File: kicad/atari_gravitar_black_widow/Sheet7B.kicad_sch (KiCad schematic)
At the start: 37 parts, among them Q10 2N3904, Q5 2N3904, Q6 2N3904, Q7 2N3906, Q8 2N3904, Q9 2N3904

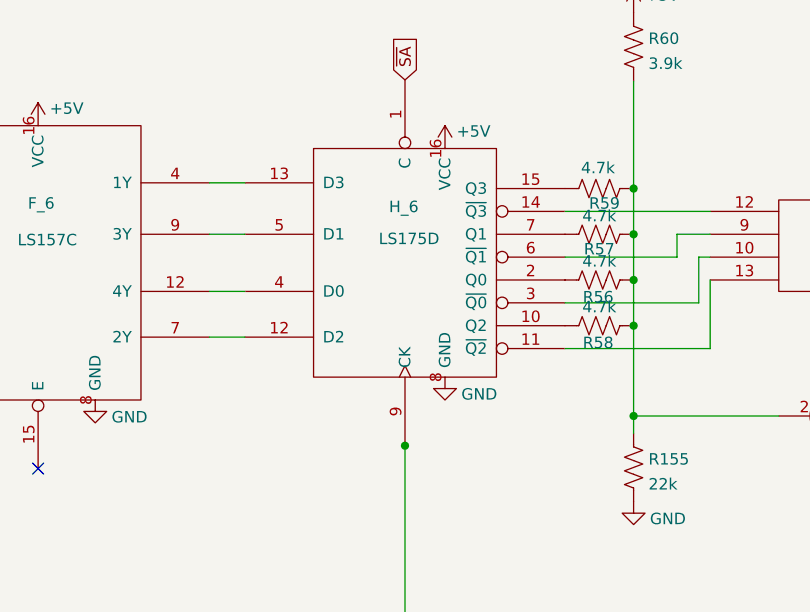
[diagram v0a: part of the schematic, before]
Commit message: Removed more warnings - 25 warnings remain
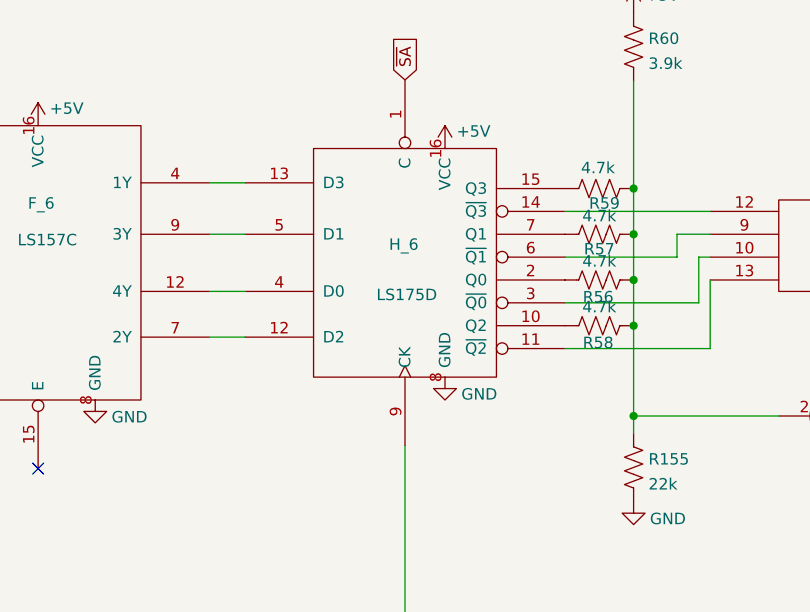
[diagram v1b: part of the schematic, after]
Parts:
- Q10, Q5, Q6, Q7, Q8, Q9: footprint TO_SOT_Packages_THT:TO-92_Molded_Narrow -> (none)

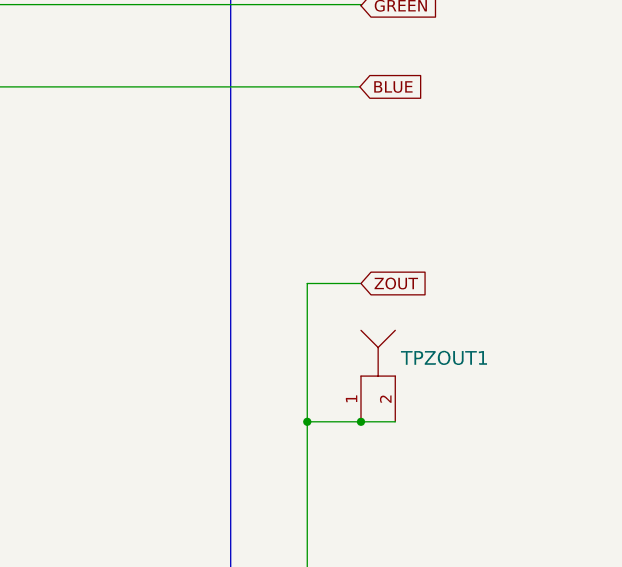
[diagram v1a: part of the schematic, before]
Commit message: 20 warnings left kicad 6.0
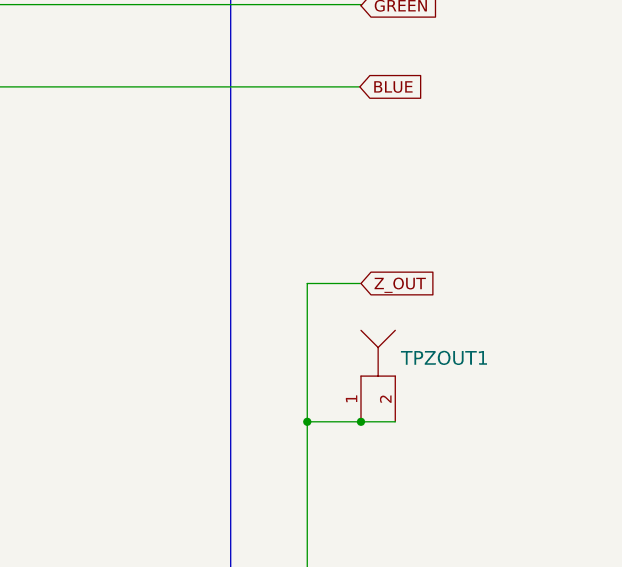
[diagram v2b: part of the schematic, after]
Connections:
- net ZOUT renamed Z_OUT
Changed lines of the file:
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@@
     )
   )
-  (global_label "ZOUT" (shape input) (at 521.208 181.356 0) (fields_autoplaced)
+  (global_label "Z_OUT" (shape input) (at 521.208 181.356 0) (fields_autoplaced)
     (effects (font (size 1.27 1.27)) (justify left))
-    (property "Intersheet References" "${INTERSHEET_REFS}" (id 0) (at 528.3703 181.2766 0)
+    (property "Intersheet References" "${INTERSHEET_REFS}" (id 0) (at 529.3379 181.2766 0)
       (effects (font (size 1.27 1.27)) (justify left) hide)
     )

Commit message: all warnings mitigated!!
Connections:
- net ~{Z0} is gone; now on net Z0: F_5.13
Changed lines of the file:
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@@
     )
   )
-  (global_label "~{Z0}" (shape input) (at 40.64 269.113 180) (fields_autoplaced)
+  (global_label "Z0" (shape input) (at 40.64 269.113 180) (fields_autoplaced)
     (effects (font (size 1.27 1.27)) (justify right))
     (property "Intersheet References" "${INTERSHEET_REFS}" (id 0) (at 35.8968 269.0336 0)

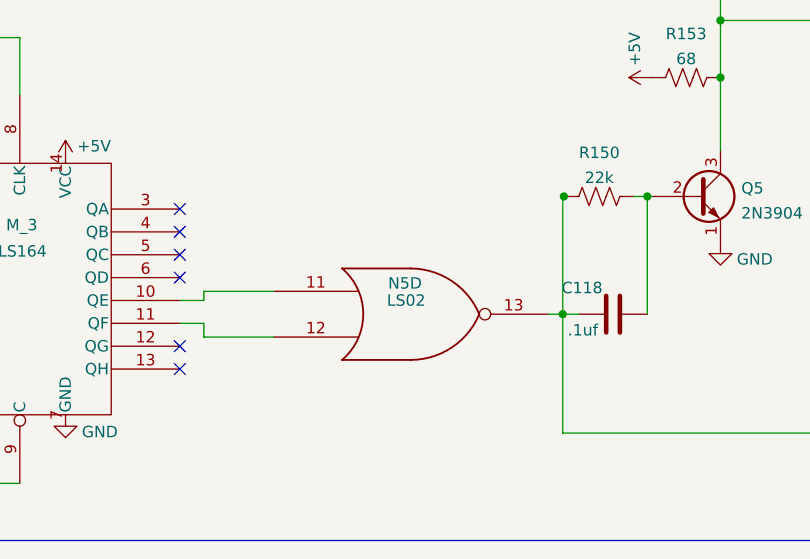
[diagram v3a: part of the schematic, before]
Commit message: Fixed all warnings and errors
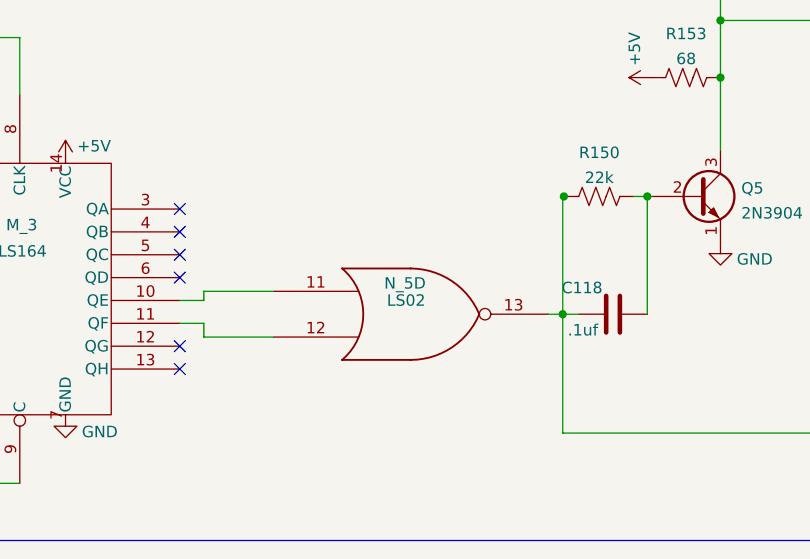
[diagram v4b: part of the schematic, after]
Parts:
- renumbered N5 to N_5
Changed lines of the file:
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@@
   (symbol (lib_id "Asteroids:LS02") (at 188.722 308.229 0) (unit 4)
     (in_bom yes) (on_board yes)
-    (property "Reference" "N5" (id 0) (at 188.087 304.8 0))
+    (property "Reference" "N_5" (id 0) (at 188.087 304.8 0))
     (property "Value" "LS02" (id 1) (at 188.214 306.705 0))
     (property "Footprint" "" (id 2) (at 188.722 308.229 0)

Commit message: more ttl placements
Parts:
- E_6, F_6, H_6: footprint (none) -> Star_Wars_Vector_PCB:DIP16
- F_5, H_5: footprint (none) -> Star_Wars_Vector_PCB:DIP14
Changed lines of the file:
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@@
       (effects (font (size 1.27 1.27)) (justify left))
     )
-    (property "Footprint" "" (id 2) (at 73.914 231.013 0)
+    (property "Footprint" "Star_Wars_Vector_PCB:DIP16" (id 2) (at 73.914 231.013 0)
       (effects (font (size 1.27 1.27)) hide)
     )
@@
       (effects (font (size 1.27 1.27)) (justify left))
     )
-    (property "Footprint" "" (id 2) (at 121.793 232.283 0)
+    (property "Footprint" "Star_Wars_Vector_PCB:DIP16" (id 2) (at 121.793 232.283 0)
       (effects (font (size 1.27 1.27)) hide)
     )
@@
     (property "Reference" "F_5" (id 0) (at 91.821 263.906 0))
     (property "Value" "LS11" (id 1) (at 91.694 266.827 0))
-    (property "Footprint" "" (id 2) (at 92.202 265.303 0)
+    (property "Footprint" "Star_Wars_Vector_PCB:DIP14" (id 2) (at 92.202 265.303 0)
       (effects (font (size 1.27 1.27)) hide)
     )
@@
       (effects (font (size 1.27 1.27)) (justify left))
     )
-    (property "Footprint" "" (id 2) (at 162.56 231.648 0)
+    (property "Footprint" "Star_Wars_Vector_PCB:DIP16" (id 2) (at 162.56 231.648 0)
       (effects (font (size 1.27 1.27)) hide)
     )
@@
     (property "Reference" "H_5" (id 0) (at 211.455 227.584 0))
     (property "Value" "LS20" (id 1) (at 211.455 229.997 0))
-    (property "Footprint" "" (id 2) (at 211.709 230.378 0)
-      (effects (font (size 1.27 1.27)) hide)
-    )
+    (property "Footprint" "Star_Wars_Vector_PCB:DIP14" (id 2) (at 211.709 230.378 0)
+      (effects (font (size 1.27 1.27)) hide)
+    )

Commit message: more chip layouts
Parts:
- J_3: footprint (none) -> Star_Wars_Vector_PCB:DIP14
- K_10: footprint (none) -> Star_Wars_Vector_PCB:DIP16
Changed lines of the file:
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@@
       (effects (font (size 1.27 1.27)) (justify left))
     )
-    (property "Footprint" "" (id 2) (at 330.073 207.772 0)
+    (property "Footprint" "Star_Wars_Vector_PCB:DIP16" (id 2) (at 330.073 207.772 0)
       (effects (font (size 1.27 1.27)) hide)
     )
@@
     (property "Reference" "J_3" (id 0) (at 245.364 225.425 0))
     (property "Value" "LS04" (id 1) (at 245.364 227.711 0))
-    (property "Footprint" "" (id 2) (at 242.189 230.378 0)
-      (effects (font (size 1.27 1.27)) hide)
-    )
+    (property "Footprint" "Star_Wars_Vector_PCB:DIP14" (id 2) (at 242.189 230.378 0)
+      (effects (font (size 1.27 1.27)) hide)
+    )

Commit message: placements
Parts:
- L_10, M_3, M_5, N_5: footprint (none) -> Star_Wars_Vector_PCB:DIP14
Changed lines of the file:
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@@
     (property "Reference" "L_10" (id 0) (at 362.839 201.2655 0))
     (property "Value" "74LS33" (id 1) (at 362.839 204.0406 0))
-    (property "Footprint" "" (id 2) (at 362.839 209.042 0)
+    (property "Footprint" "Star_Wars_Vector_PCB:DIP14" (id 2) (at 362.839 209.042 0)
       (effects (font (size 1.27 1.27)) hide)
     )
@@
     (property "Reference" "L_10" (id 0) (at 362.839 214.8545 0))
     (property "Value" "74LS33" (id 1) (at 362.839 217.6296 0))
-    (property "Footprint" "" (id 2) (at 362.839 222.631 0)
+    (property "Footprint" "Star_Wars_Vector_PCB:DIP14" (id 2) (at 362.839 222.631 0)
       (effects (font (size 1.27 1.27)) hide)
     )
@@
     (property "Reference" "L_10" (id 0) (at 362.966 228.5705 0))
     (property "Value" "74LS33" (id 1) (at 362.966 231.3456 0))
-    (property "Footprint" "" (id 2) (at 362.966 236.347 0)
+    (property "Footprint" "Star_Wars_Vector_PCB:DIP14" (id 2) (at 362.966 236.347 0)
       (effects (font (size 1.27 1.27)) hide)
     )
@@
     (property "Reference" "N_5" (id 0) (at 188.087 304.8 0))
     (property "Value" "LS02" (id 1) (at 188.214 306.705 0))
-    (property "Footprint" "" (id 2) (at 188.722 308.229 0)
+    (property "Footprint" "Star_Wars_Vector_PCB:DIP14" (id 2) (at 188.722 308.229 0)
       (effects (font (size 1.27 1.27)) hide)
     )
@@
       (effects (font (size 1.27 1.27)) (justify left))
     )
-    (property "Footprint" "" (id 2) (at 145.288 305.435 0)
+    (property "Footprint" "Star_Wars_Vector_PCB:DIP14" (id 2) (at 145.288 305.435 0)
       (effects (font (size 1.27 1.27)) hide)
     )
@@
     (property "Reference" "M_5" (id 0) (at 333.756 254.381 0))
     (property "Value" "LS32" (id 1) (at 333.756 257.302 0))
-    (property "Footprint" "" (id 2) (at 334.137 256.159 0)
-      (effects (font (size 1.27 1.27)) hide)
-    )
+    (property "Footprint" "Star_Wars_Vector_PCB:DIP14" (id 2) (at 334.137 256.159 0)
+      (effects (font (size 1.27 1.27)) hide)
+    )

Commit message: TEST POINTS PLACED
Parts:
- TPBLUE1, TPGREEN1, TPRED1, TPZOUT1: footprint (none) -> quantum_arcade_pcb:TP
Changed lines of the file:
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@@
       (effects (font (size 1.524 1.524)) hide)
     )
-    (property "Footprint" "" (id 2) (at 530.479 130.048 0)
+    (property "Footprint" "quantum_arcade_pcb:TP" (id 2) (at 530.479 130.048 0)
       (effects (font (size 1.524 1.524)) hide)
     )
@@
       (effects (font (size 1.524 1.524)) hide)
     )
-    (property "Footprint" "" (id 2) (at 521.208 192.913 0)
+    (property "Footprint" "quantum_arcade_pcb:TP" (id 2) (at 521.208 192.913 0)
       (effects (font (size 1.524 1.524)) hide)
     )
@@
       (effects (font (size 1.524 1.524)) hide)
     )
-    (property "Footprint" "" (id 2) (at 521.208 136.144 0)
+    (property "Footprint" "quantum_arcade_pcb:TP" (id 2) (at 521.208 136.144 0)
       (effects (font (size 1.524 1.524)) hide)
     )
@@
       (effects (font (size 1.524 1.524)) hide)
     )
-    (property "Footprint" "" (id 2) (at 521.208 124.587 0)
-      (effects (font (size 1.524 1.524)) hide)
-    )
+    (property "Footprint" "quantum_arcade_pcb:TP" (id 2) (at 521.208 124.587 0)
+      (effects (font (size 1.524 1.524)) hide)
+    )
